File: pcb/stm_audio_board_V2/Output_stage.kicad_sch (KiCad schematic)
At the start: 24 parts, among them U6 AD1934, U7 OP275

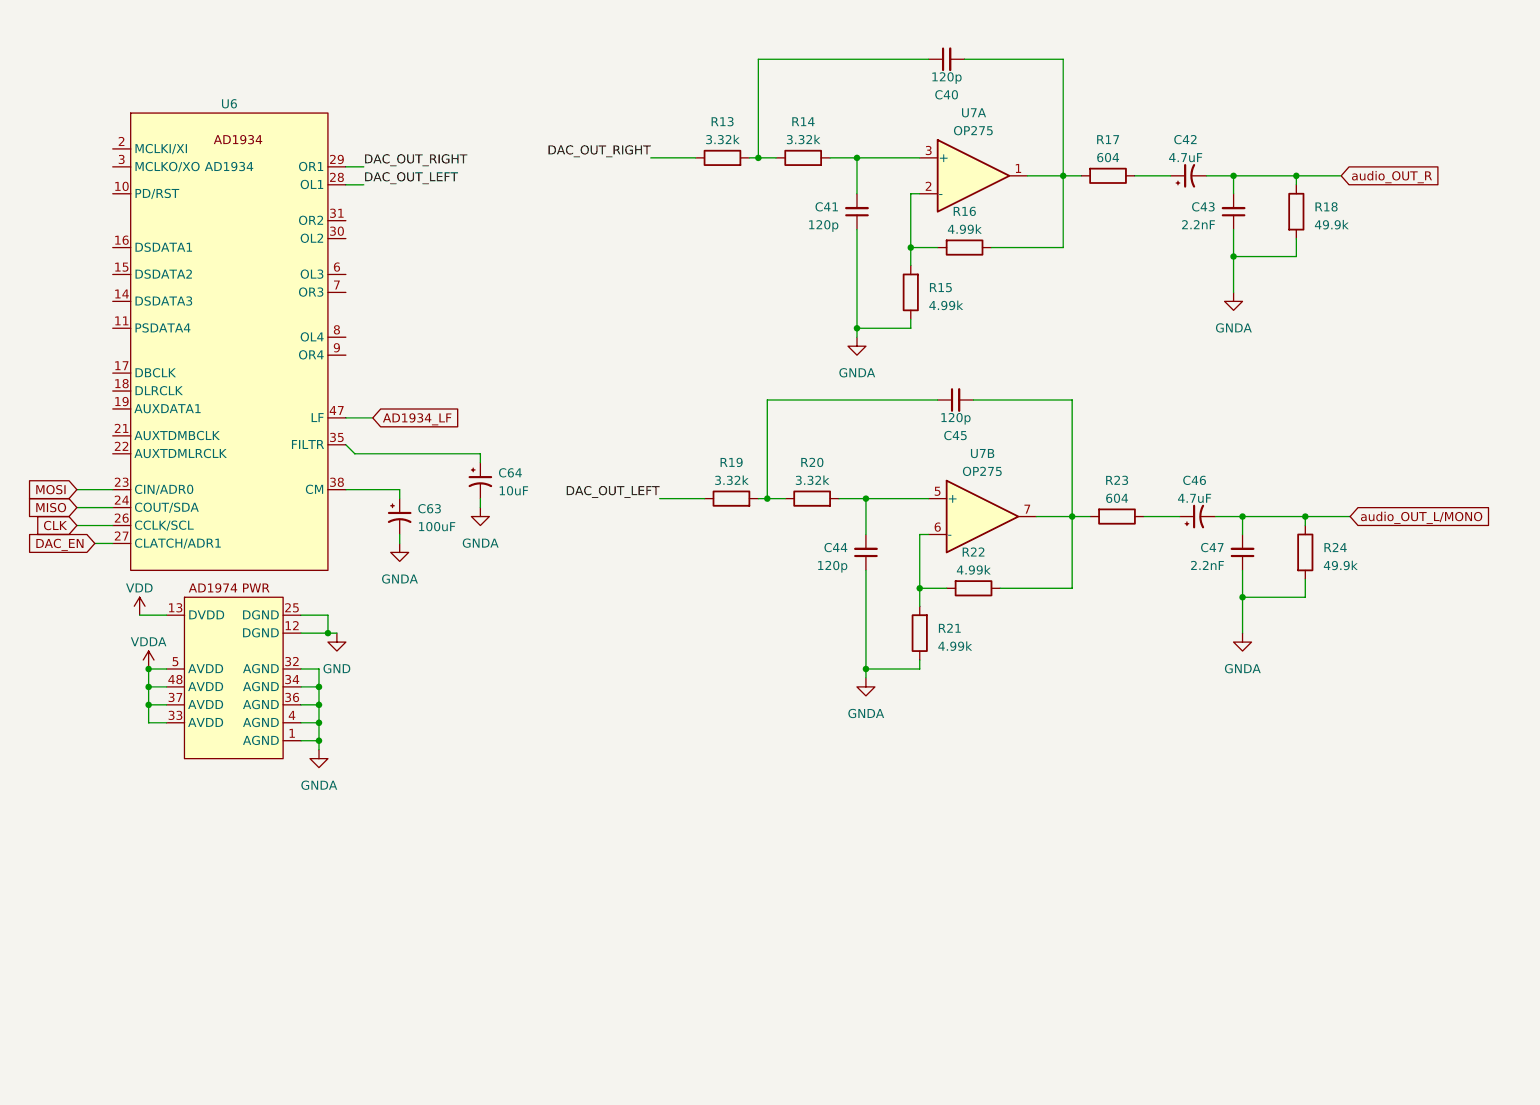
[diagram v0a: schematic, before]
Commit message: added choke to analog pwr, created 5 V rail, decided to pivot and use codec instead dedicated hardware
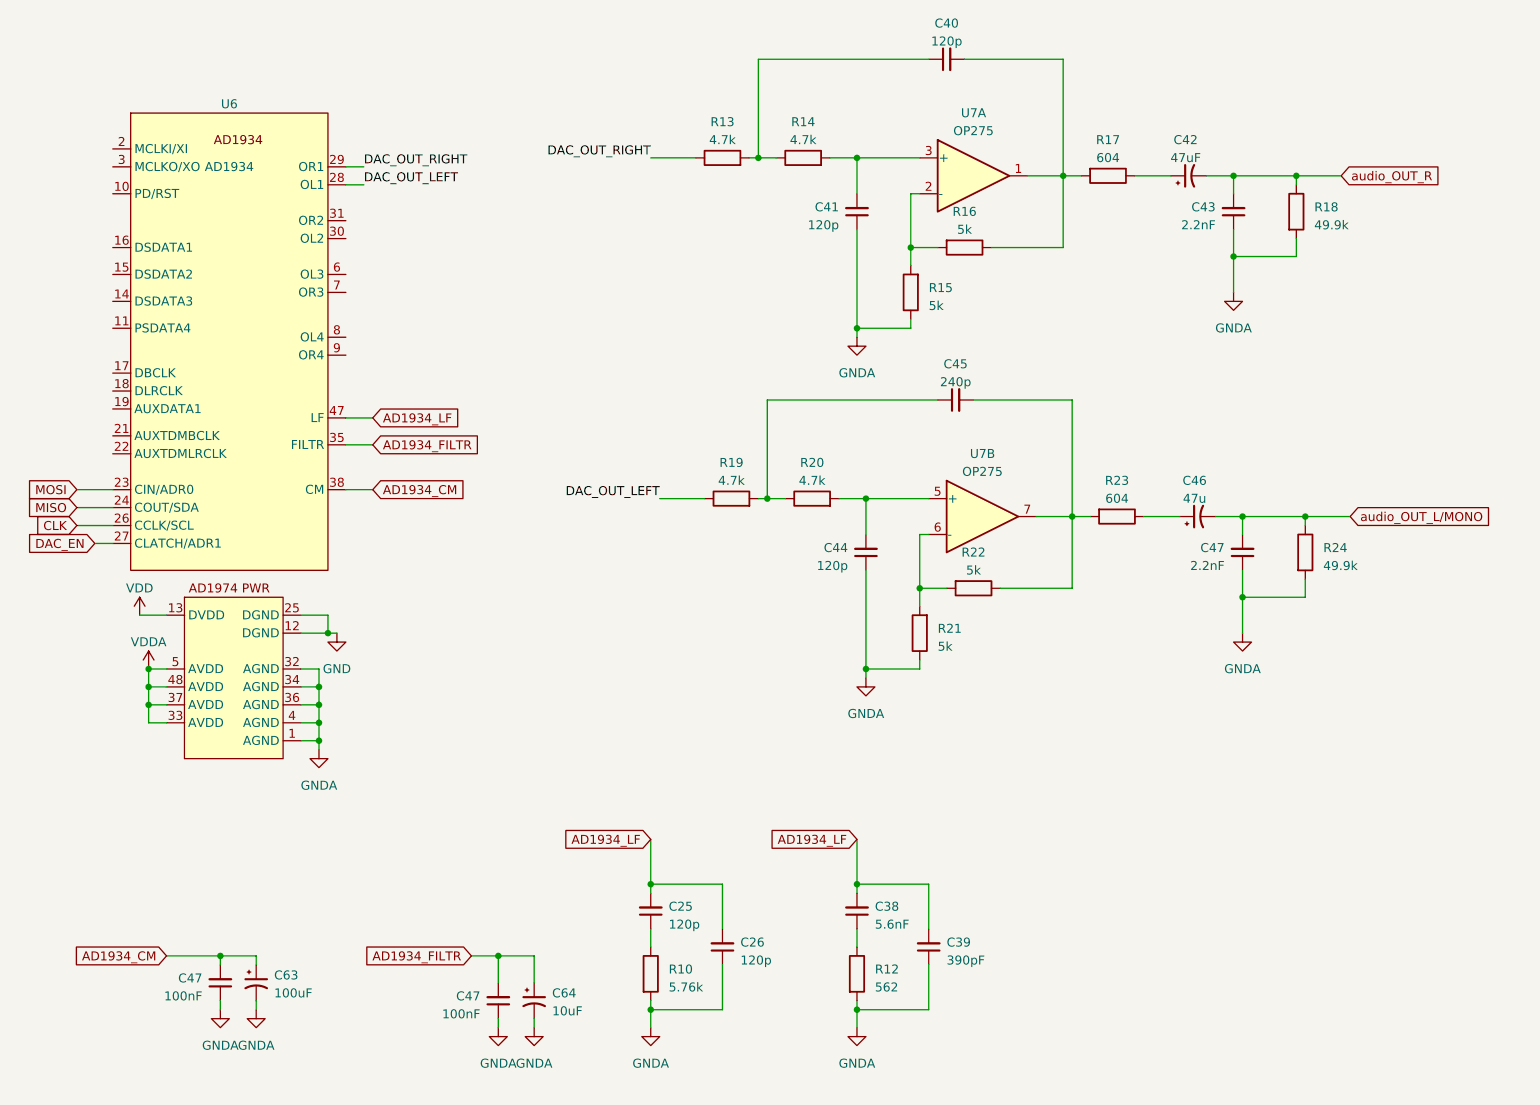
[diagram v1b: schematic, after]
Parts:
- added C25, C26: 120p, Capacitor_SMD:C_0603_1608Metric_Pad1.08x0.95mm_HandSolder, symbol Device:C_Small
- added C38: 5.6nF, Capacitor_SMD:C_0603_1608Metric_Pad1.08x0.95mm_HandSolder, symbol Device:C_Small
- added C39: 390pF, Capacitor_SMD:C_0603_1608Metric_Pad1.08x0.95mm_HandSolder, symbol Device:C_Small
- added C47 (x2): 100nF, Capacitor_SMD:C_0603_1608Metric_Pad1.08x0.95mm_HandSolder, symbol Device:C_Small
- added R10: 5.76k, Resistor_SMD:R_0805_2012Metric_Pad1.20x1.40mm_HandSolder, symbol Device:R
- added R12: 562, Resistor_SMD:R_0805_2012Metric_Pad1.20x1.40mm_HandSolder, symbol Device:R
- C42: value 4.7uF -> 47uF
- C45: value 120p -> 240p
- C46: value 4.7uF -> 47u
- R13, R14, R19, R20: value 3.32k -> 4.7k
- R15, R16, R21, R22: value 4.99k -> 5k
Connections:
- net AD1934_LF: now also C25.2, C26.2, C38.2, C39.2
- net GNDA: now also C26.1, C39.1, C47.1, C47.1, R10.2, R12.2
- net AD1934_FILTR: now reaches C64.1, U6.35 (FILTR)
- net AD1934_FILTR: now also C47.2
- net AD1934_CM: now reaches C63.1, U6.38 (CM)
- net AD1934_CM: now also C47.2
- new net: C38.1, R12.1
- new net: C25.1, R10.1

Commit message: testing offset sim, and changing layout
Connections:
- net audio_OUT_L/MONO renamed GUITAR_OUT_L/MONO
- net audio_OUT_R renamed GUITAR_OUT_R
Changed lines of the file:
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@@
     (effects (font (size 1.27 1.27)) (justify left bottom))
   )
-  (global_label "audio_OUT_L{slash}MONO" (shape input) (at 214.63 110.49 0) (fields_autoplaced)
+  (global_label "GUITAR_OUT_L{slash}MONO" (shape input) (at 213.36 110.49 0) (fields_autoplaced)
     (effects (font (size 1.27 1.27)) (justify left))
-    (property "Intersheetrefs" "${INTERSHEET_REFS}" (at 236.1019 110.49 0)
+    (property "Intersheetrefs" "${INTERSHEET_REFS}" (at 236.1626 110.49 0)
       (effects (font (size 1.27 1.27)) (justify left) hide)
     )
@@
     )
   )
-  (global_label "audio_OUT_R" (shape input) (at 213.36 62.23 0) (fields_autoplaced)
+  (global_label "GUITAR_OUT_R" (shape input) (at 213.36 62.23 0) (fields_autoplaced)
     (effects (font (size 1.27 1.27)) (justify left))
-    (property "Intersheetrefs" "${INTERSHEET_REFS}" (at 228.3004 62.23 0)
+    (property "Intersheetrefs" "${INTERSHEET_REFS}" (at 229.6311 62.23 0)
       (effects (font (size 1.27 1.27)) (justify left) hide)
     )

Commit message: Update AD1939_input_with_offset.asc, AD1939_input_with_offset.log, and 8 more files...
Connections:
- net GNDA is gone; now on net GND: C26.1, C39.1, C41.1, C43.1, C44.1, C47.1, C47.1, C47.1, C63.2, C64.2, R10.2, R12.2, R15.1, R18.2, R21.1, R24.2, U6.1 (AGND), U6.32 (AGND), U6.34 (AGND), U6.36 (AGND), U6.4 (AGND)

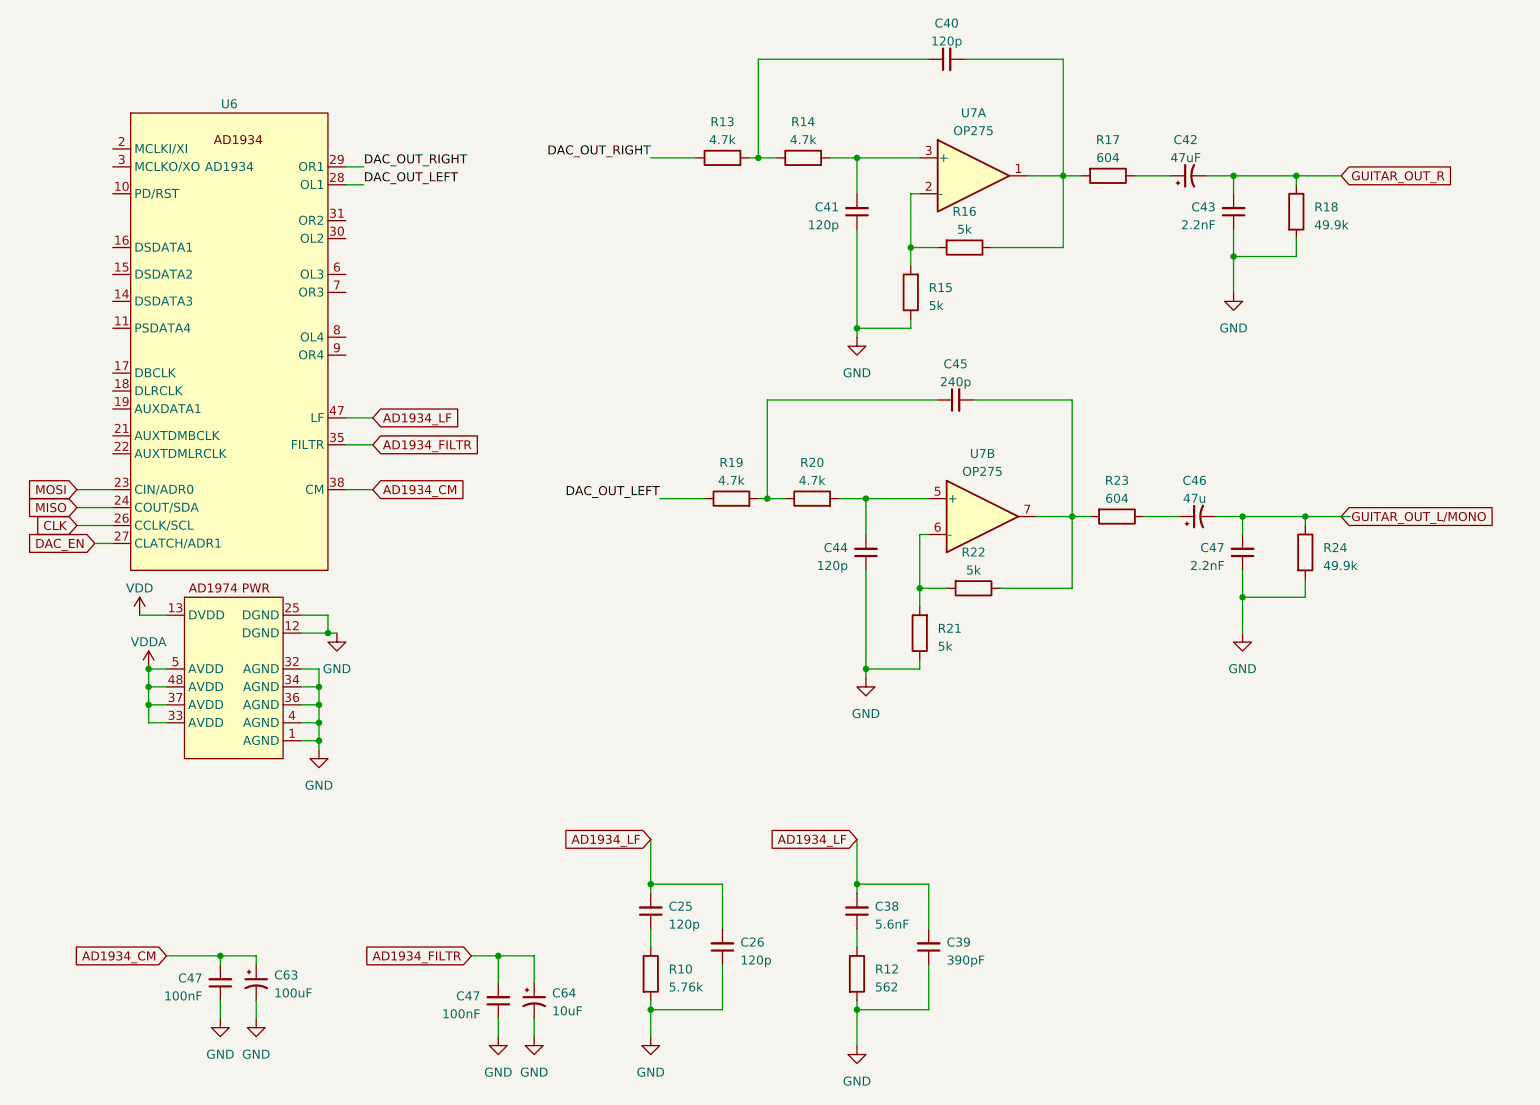
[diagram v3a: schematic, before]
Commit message: input and output stage reworked in sim and in schematic, power filtering is changed, further calculations needed
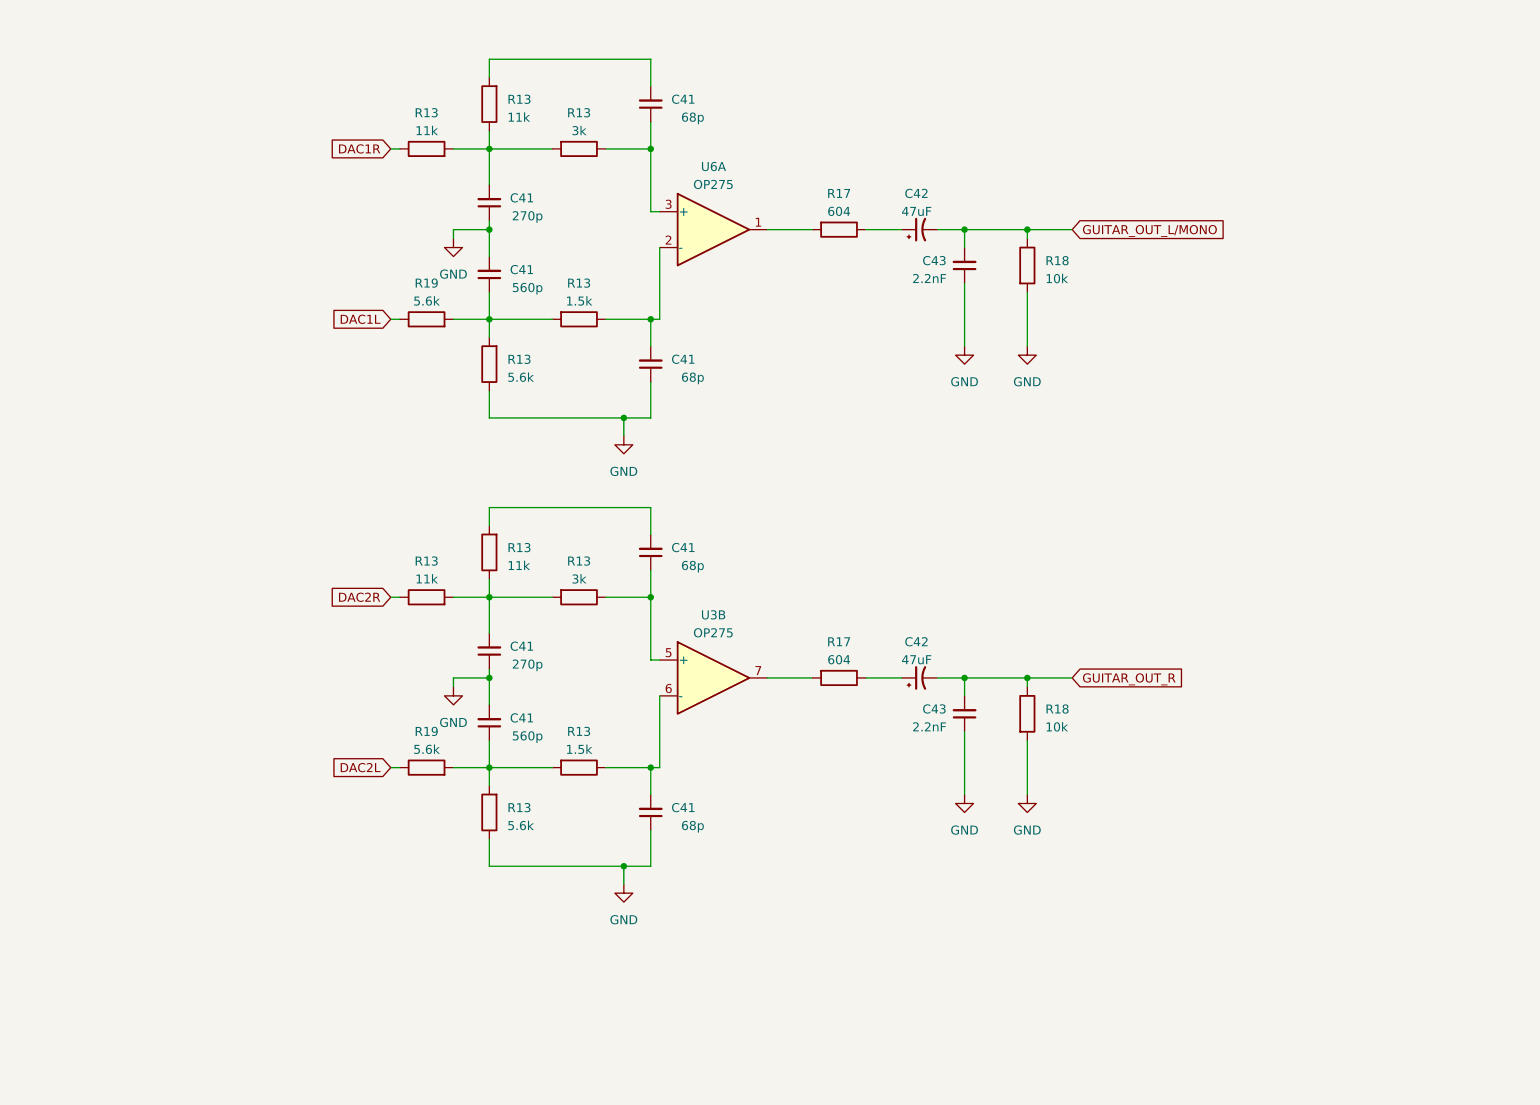
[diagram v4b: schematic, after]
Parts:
- removed C25, C26, C40, C41, C44: 120p, Capacitor_SMD:C_0603_1608Metric_Pad1.08x0.95mm_HandSolder, symbol Device:C_Small
- removed C38: 5.6nF, Capacitor_SMD:C_0603_1608Metric_Pad1.08x0.95mm_HandSolder, symbol Device:C_Small
- removed C39: 390pF, Capacitor_SMD:C_0603_1608Metric_Pad1.08x0.95mm_HandSolder, symbol Device:C_Small
- removed C45: 240p, Capacitor_SMD:C_0603_1608Metric_Pad1.08x0.95mm_HandSolder, symbol Device:C_Small
- removed C46: 47u, Capacitor_SMD:C_0805_2012Metric_Pad1.18x1.45mm_HandSolder, symbol Device:C_Polarized_Small_US
- removed C47 (x2): 100nF, Capacitor_SMD:C_0603_1608Metric_Pad1.08x0.95mm_HandSolder, symbol Device:C_Small
- removed C47: 2.2nF, Capacitor_SMD:C_0603_1608Metric_Pad1.08x0.95mm_HandSolder, symbol Device:C_Small
- removed C63: 100uF, Capacitor_SMD:C_1210_3225Metric_Pad1.33x2.70mm_HandSolder, symbol Device:C_Polarized_Small_US
- removed C64: 10uF, Capacitor_SMD:C_1210_3225Metric_Pad1.33x2.70mm_HandSolder, symbol Device:C_Polarized_Small_US
- removed R10: 5.76k, Resistor_SMD:R_0805_2012Metric_Pad1.20x1.40mm_HandSolder, symbol Device:R
- removed R12: 562, Resistor_SMD:R_0805_2012Metric_Pad1.20x1.40mm_HandSolder, symbol Device:R
- removed R13, R14, R19, R20: 4.7k, Resistor_SMD:R_0805_2012Metric_Pad1.20x1.40mm_HandSolder, symbol Device:R
- removed R15, R16, R21, R22: 5k, Resistor_SMD:R_0805_2012Metric_Pad1.20x1.40mm_HandSolder, symbol Device:R
- removed R23: 604, Resistor_SMD:R_0805_2012Metric_Pad1.20x1.40mm_HandSolder, symbol Device:R
- removed R24: 49.9k, Resistor_SMD:R_0805_2012Metric_Pad1.20x1.40mm_HandSolder, symbol Device:R
- removed U6: AD1934, Package_QFP:LQFP-48_7x7mm_P0.5mm, symbol stm_audio:AD1934
- removed U7: OP275, Package_SO:SSOP-8_3.9x5.05mm_P1.27mm, symbol Amplifier_Operational:OP275
- added C41 (x2): 560p, Capacitor_SMD:C_0603_1608Metric_Pad1.08x0.95mm_HandSolder, symbol Device:C_Small
- added C41 (x4): 68p, Capacitor_SMD:C_0603_1608Metric_Pad1.08x0.95mm_HandSolder, symbol Device:C_Small
- added C41 (x2): 270p, Capacitor_SMD:C_0603_1608Metric_Pad1.08x0.95mm_HandSolder, symbol Device:C_Small
- added C42: 47uF, Capacitor_SMD:C_0805_2012Metric_Pad1.18x1.45mm_HandSolder, symbol Device:C_Polarized_Small_US
- added C43: 2.2nF, Capacitor_SMD:C_0603_1608Metric_Pad1.08x0.95mm_HandSolder, symbol Device:C_Small
- added R13 (x2): 3k, Resistor_SMD:R_0805_2012Metric_Pad1.20x1.40mm_HandSolder, symbol Device:R
- added R13 (x4): 11k, Resistor_SMD:R_0805_2012Metric_Pad1.20x1.40mm_HandSolder, symbol Device:R
- added R13 (x2), R19 (x2): 5.6k, Resistor_SMD:R_0805_2012Metric_Pad1.20x1.40mm_HandSolder, symbol Device:R
- added R13 (x2): 1.5k, Resistor_SMD:R_0805_2012Metric_Pad1.20x1.40mm_HandSolder, symbol Device:R
- added R17: 604, Resistor_SMD:R_0805_2012Metric_Pad1.20x1.40mm_HandSolder, symbol Device:R
- added R18: 10k, Resistor_SMD:R_0805_2012Metric_Pad1.20x1.40mm_HandSolder, symbol Device:R
- added U3, U6: OP275, symbol Amplifier_Operational:OP275
- R18: value 49.9k -> 10k
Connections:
- net GND: now also C41.1, C41.1, C41.1, C41.1, C41.2, C41.2, C43.1, R13.1, R13.1, R18.2
- net GUITAR_OUT_L/MONO: now also C42.2, C43.2, R18.1
- net GUITAR_OUT_R: now also C42.2, C43.2, R18.1; no longer C42.2, C43.2, R18.1
- net at R17.2: now also U6.1
- new net: C41.2, R13.1, U6.2 (-)
- new net: C41.1, R13.1, U6.3 (+)
- new net: C41.1, R13.2, R13.2, R19.2 (x2)
- new net: C41.2, R13.1, R13.2, R13.2 (x2)
- new net: C41.2, R13.2 (x2)
- new net: C41.1, R13.1, U3.5 (+)
- new net: C41.2, R13.1, U3.6 (-)
- new net: R17.2, U3.7
- new net: C42.1, R17.1
- new net DAC1L: R19.1
- new net DAC1R: R13.1
- new net DAC2L: R19.1
- new net DAC2R: R13.1
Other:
- moved on the sheet: C42, C43, R17, R18
